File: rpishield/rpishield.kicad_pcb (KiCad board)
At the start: 2 copper layers, 50.4 x 41.8 mm, 16 parts, among them P1 CONN_13X2, P2 CONN_01X09, U1 ANTENNA, U2 DS1338, U3 MCP1702, X1 32.768KHz

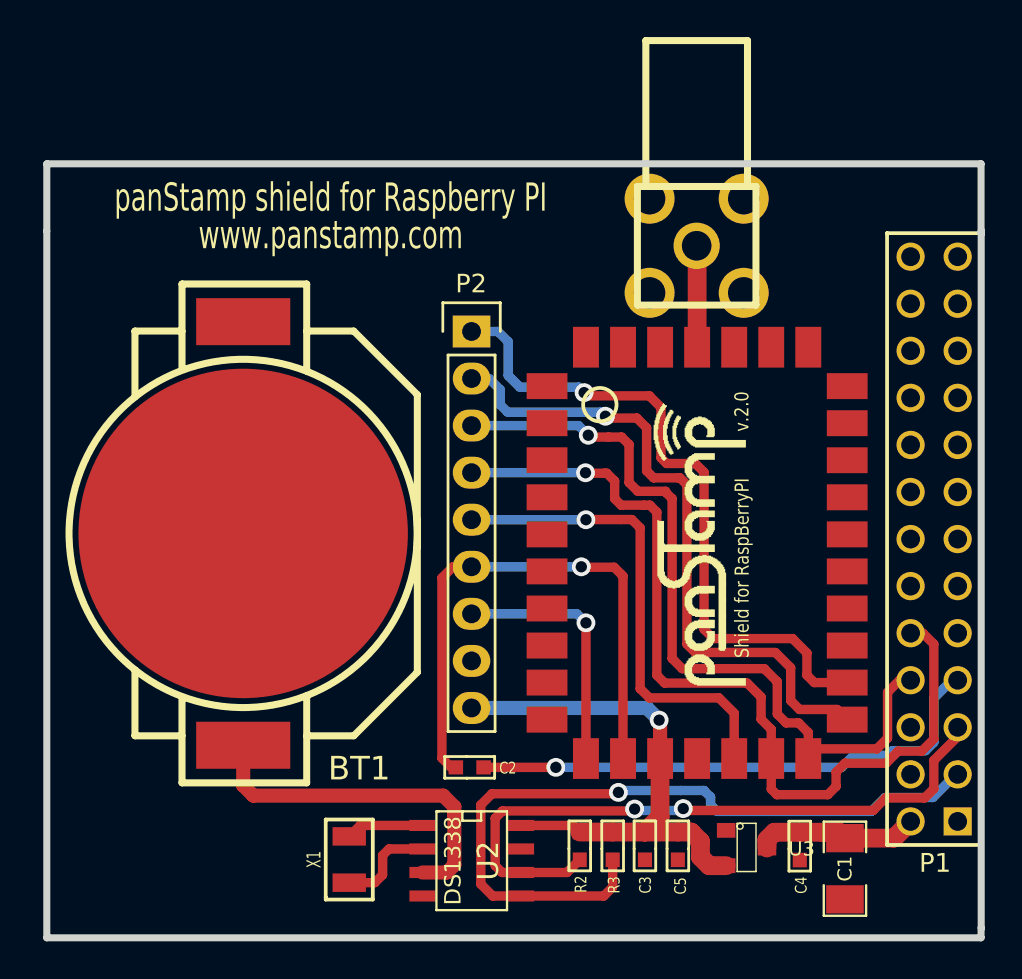
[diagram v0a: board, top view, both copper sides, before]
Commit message: RPi shield for panStamp 2 completed
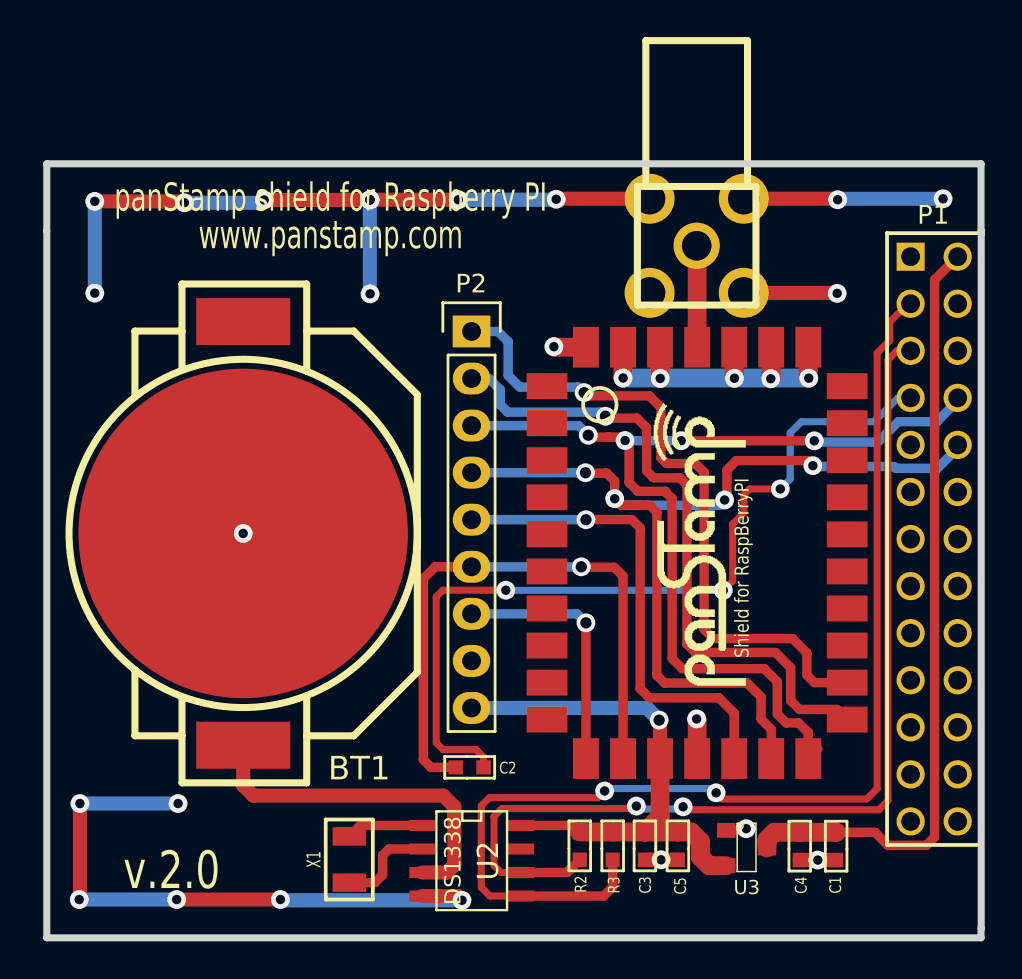
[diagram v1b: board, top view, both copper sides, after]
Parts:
- C1: value 4.7u -> 10u; footprint SM1206 -> mysmd:SM0603S
- moved C1 1.31 mm to (160.8, 91.4)
- turned P1 to 270 degrees
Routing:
- net GND: track 0.00 -> 116.9 mm, vias 0 -> 29
- net +5V: track 10.2 -> 42.0 mm
- net /RPI_I2C_SDA: track 41.0 -> 62.6 mm, vias 1 -> 2
- net /RPI_I2C_SCL: track 35.9 -> 54.8 mm
- net Net-(C2-Pad1): track 29.0 -> 45.2 mm, vias 1 -> 3
- net /RXD: track 42.5 -> 53.6 mm, vias 1 -> 4
- net /RESET: track 30.8 -> 34.0 mm
- net /TXD: track 49.0 -> 51.2 mm, vias 1 -> 4
- net Net-(P1-Pad22): track 0.00 -> 0.50 mm
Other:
- board text added: "v.2.0"

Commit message: Fiducials added to the PCB
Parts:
- added fiducial: VAL**, mymods:fiducial, F.Cu at (120.0, 94.6)
- added fiducial: VAL**, mymods:fiducial, F.Cu at (166.9, 56.1)
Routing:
- net GND: track 116.9 -> 109.7 mm, vias 29 -> 28
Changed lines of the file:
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@@
-(kicad_pcb (version 4) (host pcbnew "(2014-jul-16 BZR unknown)-product")
+(kicad_pcb (version 4) (host pcbnew no-vcs-found-product)
   (general
     (links 48)
     (no_connects 0)
-    (area 118.034499 54.359499 168.846501 96.515501)
+    (area 115.342686 47.506899 171.217314 101.7824)
     (thickness 1.6002)
     (drawings 11)
-    (tracks 360)
+    (tracks 358)
     (zones 0)
-    (modules 16)
+    (modules 18)
     (nets 56)
   )
@@
   )
   (setup
-    (last_trace_width 0.762)
+    (last_trace_width 0.254)
     (user_trace_width 0.2032)
     (user_trace_width 0.254)
@@
     (visible_elements FFFFFBFF)
     (pcbplotparams
-      (layerselection 0x00030_80000001)
+      (layerselection 0x010e0_80000001)
       (usegerberextensions true)
       (excludeedgelayer true)
@@
       (drillshape 0)
       (scaleselection 1)
-      (outputdirectory ""))
+      (outputdirectory production/))
   )
   (net 0 "")
@@
     (descr "2 x 13 pins connector")
     (tags CONN)
-    (fp_text reference P1 (at -17.4879 0.0508 360) (layer F.SilkS)
+    (fp_text reference P1 (at 17.617 -0.004 360) (layer F.SilkS)
       (effects (font (size 1.016 1.016) (thickness 0.2032)))
     )
@@
     )
   )
+  (module mymods:fiducial (layer Front)
+    (at 119.99 94.62)
+    (fp_text reference fiducial (at -0.01 3.34) (layer F.SilkS) hide
+      (effects (font (thickness 0.3048)))
+    )
+    (fp_text value VAL** (at -0.19 5.74) (layer F.SilkS) hide
+      (effects (font (thickness 0.3048)))
+    )
+    (pad 1 smd circle (at 0 0) (size 1 1) (layers Front F.Mask)
+      (solder_mask_margin 0.5) (clearance 0.5))
+  )
+  (module mymods:fiducial (layer Front)
+    (at 166.94 56.13)
+    (fp_text reference fiducial (at -0.36 -5.11) (layer F.SilkS) hide
+      (effects (font (thickness 0.3048)))
+    )
+    (fp_text value VAL** (at 0.29 -2.95) (layer F.SilkS) hide
+      (effects (font (thickness 0.3048)))
+    )
+    (pad 1 smd circle (at 0 0) (size 1 1) (layers Front F.Mask)
+      (solder_mask_margin 0.5) (clearance 0.5))
+  )
   (gr_text v.2.0 (at 124.968 92.6973) (layer F.SilkS)
     (effects (font (size 2.032 1.524) (thickness 0.3048)))
@@
   (segment (start 120.015 89.0778) (end 125.3109 89.0778) (width 0.762) (layer Back) (net 8))
   (via (at 120.015 89.0778) (size 1.016) (layers Front Back) (net 8))
-  (segment (start 120.015 94.2213) (end 120.015 89.0778) (width 0.762) (layer Front) (net 8))
-  (segment (start 119.9769 94.2594) (end 120.015 94.2213) (width 0.762) (layer Front) (net 8))
-  (via (at 119.9769 94.2594) (size 1.016) (layers Front Back) (net 8))
-  (segment (start 125.2347 94.2594) (end 119.9769 94.2594) (width 0.762) (layer Back) (net 8))
+  (segment (start 119.9881 92.2319) (end 120.015 89.0778) (width 0.762) (layer Front) (net 8))
+  (segment (start 119.95 92.27) (end 119.9881 92.2319) (width 0.762) (layer Front) (net 8))
+  (via (at 119.95 92.27) (size 1.016) (layers Front Back) (net 8))
+  (segment (start 125.2347 94.2594) (end 119.95 92.27) (width 0.762) (layer Back) (net 8))
   (via (at 125.2347 94.2594) (size 1.016) (layers Front Back) (net 8))
   (via (at 151.37892 92.1131) (size 1.016) (layers Front Back) (net 8))
@@
   (segment (start 160.8544 61.515) (end 160.8836 61.5442) (width 0.762) (layer Front) (net 8))
   (segment (start 155.84 56.435) (end 160.8544 56.435) (width 0.762) (layer Front) (net 8))
-  (via (at 166.5986 56.4388) (size 1.016) (layers Front Back) (net 8))
-  (segment (start 160.9598 56.4388) (end 166.5986 56.4388) (width 0.762) (layer Back) (net 8))
   (segment (start 160.909 56.4896) (end 160.9598 56.4388) (width 0.762) (layer Back) (net 8))
   (via (at 160.909 56.4896) (size 1.016) (layers Front Back) (net 8))

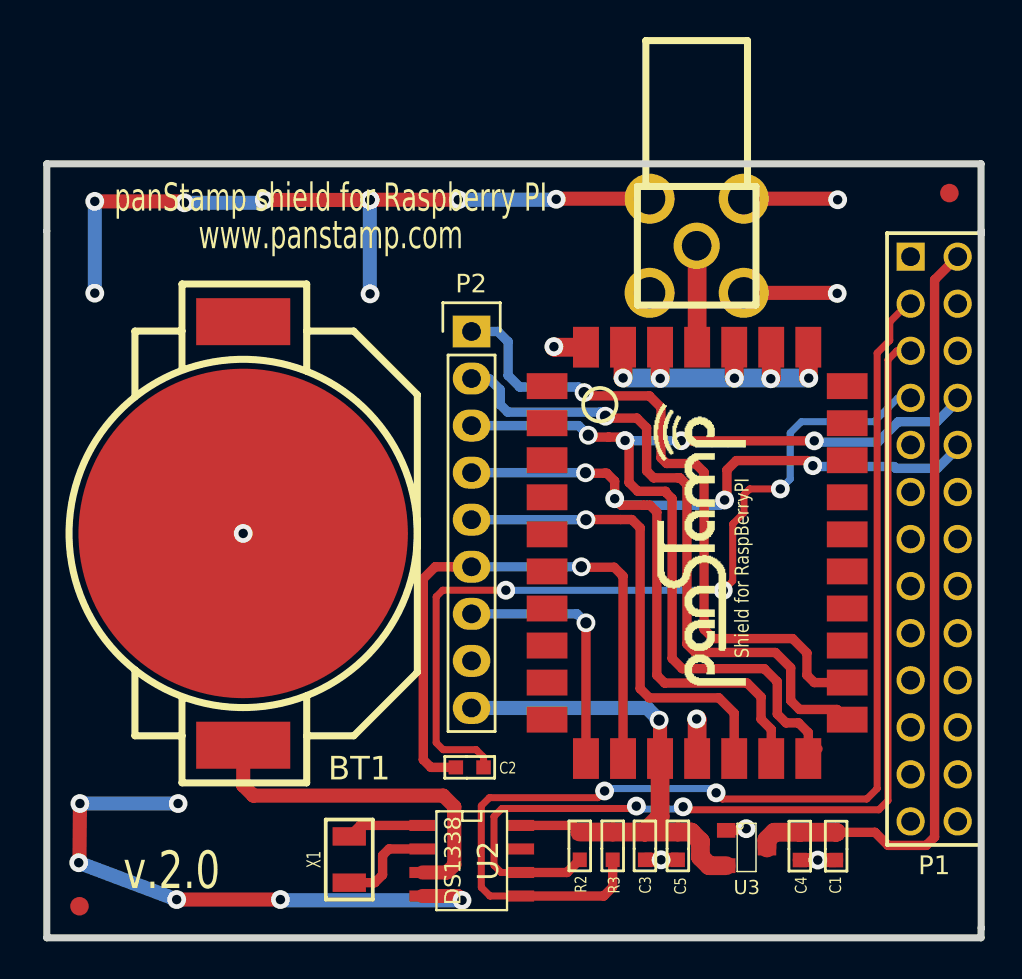
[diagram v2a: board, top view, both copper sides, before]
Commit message: Board corners rounded
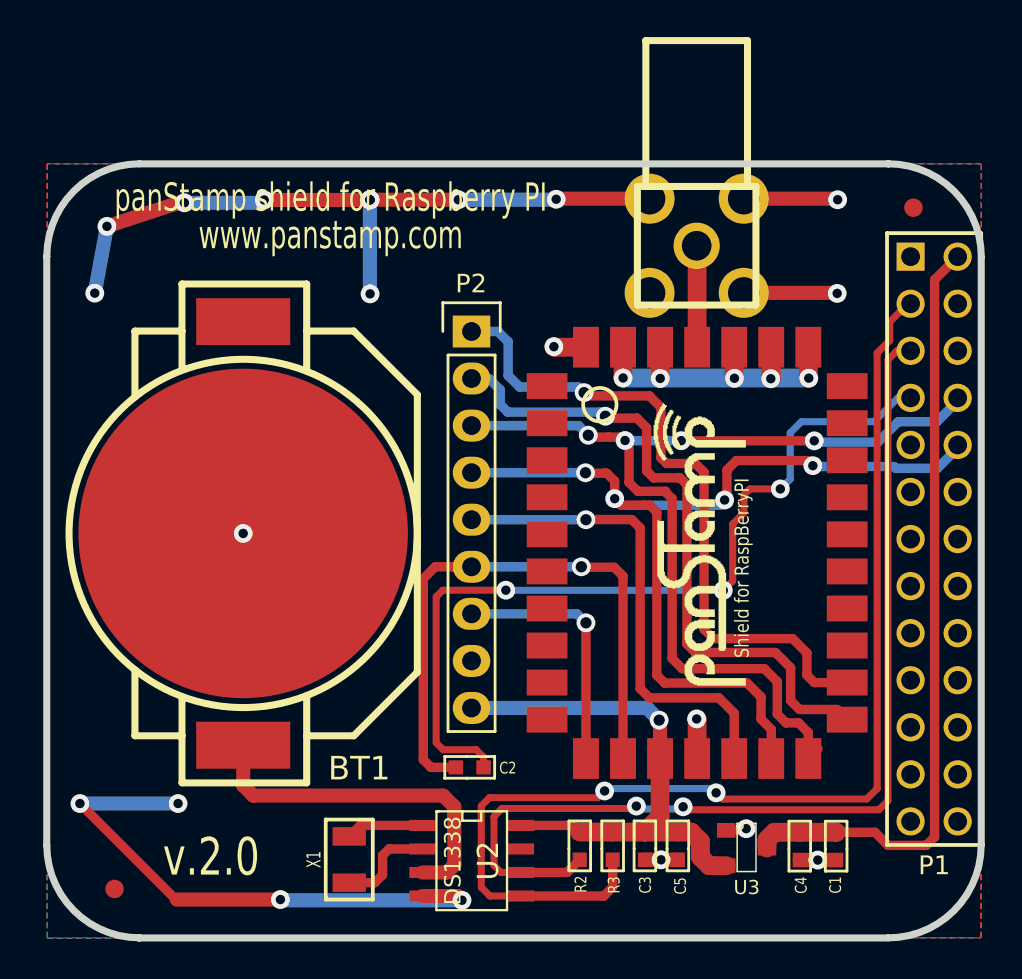
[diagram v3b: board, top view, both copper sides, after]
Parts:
- moved fiducial 2.11 mm to (121.9, 93.7)
- moved fiducial 2.10 mm to (165.0, 56.9)
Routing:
- net GND: track 109.7 -> 106.5 mm, vias 28 -> 26
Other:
- outline, holes or cut-outs redrawn
